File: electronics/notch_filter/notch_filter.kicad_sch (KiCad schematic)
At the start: 39 parts, among them J1 Conn_01x03, J2 Conn_01x03, J3 Output, J4 In, J5 module_2x15_left_input, J6 module_2x15_right_input, U1 opamp_single_8pin

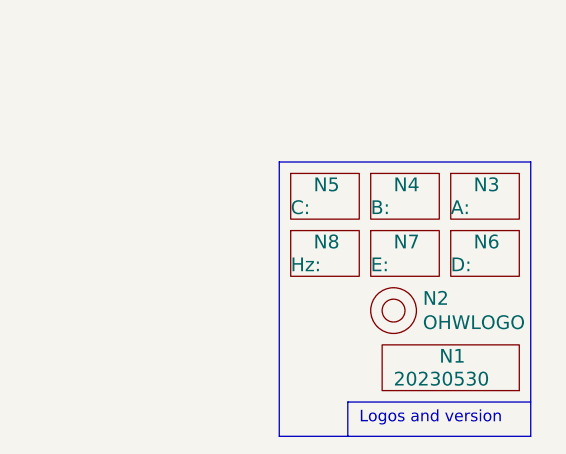
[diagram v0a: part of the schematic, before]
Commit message: removed labels and minor optimisations
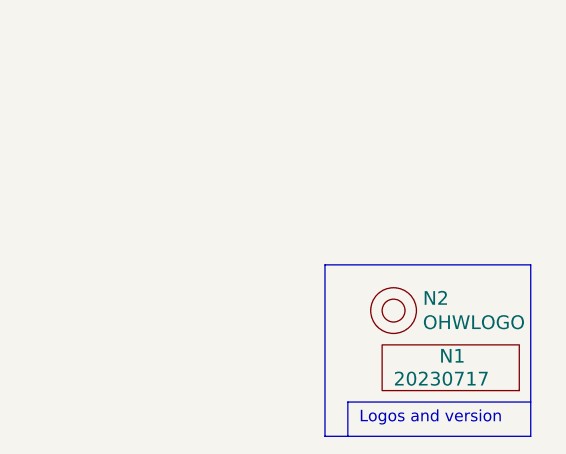
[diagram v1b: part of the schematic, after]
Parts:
- removed N3: A:, SquantorLabels:Label_Note_medium, symbol SquantorLabels:Label
- removed N4: B:, SquantorLabels:Label_Note_medium, symbol SquantorLabels:Label
- removed N5: C:, SquantorLabels:Label_Note_medium, symbol SquantorLabels:Label
- removed N6: D:, SquantorLabels:Label_Note_medium, symbol SquantorLabels:Label
- removed N7: E:, SquantorLabels:Label_Note_medium, symbol SquantorLabels:Label
- removed N8: Hz:, SquantorLabels:Label_Note_medium, symbol SquantorLabels:Label
- N1: value 20230530 -> 20230717
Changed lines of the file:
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@@
     (stroke (width 0) (type default))
   )
-  (polyline (pts (xy 147.32 165.1) (xy 147.32 195.58))
+  (polyline (pts (xy 152.4 176.53) (xy 152.4 195.58))
     (stroke (width 0) (type default))
   )
@@
     (stroke (width 0) (type default))
   )
-  (polyline (pts (xy 175.26 165.1) (xy 147.32 165.1))
+  (polyline (pts (xy 175.26 176.53) (xy 152.4 176.53))
     (stroke (width 0) (type default))
   )
@@
     (stroke (width 0) (type default))
   )
-  (polyline (pts (xy 175.26 195.58) (xy 175.26 165.1))
+  (polyline (pts (xy 175.26 195.58) (xy 175.26 176.53))
     (stroke (width 0) (type default))
   )
@@
     (stroke (width 0) (type default))
   )
-  (polyline (pts (xy 147.32 195.58) (xy 175.26 195.58))
+  (polyline (pts (xy 152.4 195.58) (xy 175.26 195.58))
     (stroke (width 0) (type default))
   )
@@
       (effects (font (size 1.524 1.524)) (justify left))
     )
-    (property "Value" "20230530" (at 160.02 189.23 0)
+    (property "Value" "20230717" (at 160.02 189.23 0)
       (effects (font (size 1.524 1.524)) (justify left))
     )
@@
         (path "/646d9e91-59b4-4865-a2fc-29780ed32563"
           (reference "R2") (unit 1)
-        )
-      )
-    )
-  )
-  (symbol (lib_id "SquantorLabels:Label") (at 152.4 175.26 0) (unit 1)
-    (in_bom yes) (on_board yes) (dnp no)
-    (property "Reference" "N8" (at 151.13 173.99 0)
-      (effects (font (size 1.524 1.524)) (justify left))
-    )
-    (property "Value" "Hz:" (at 148.59 176.53 0)
-      (effects (font (size 1.524 1.524)) (justify left))
-    )
-    (property "Footprint" "SquantorLabels:Label_Note_medium" (at 152.4 175.26 0)
-      (effects (font (size 1.524 1.524)) hide)
-    )
-    (property "Datasheet" "" (at 152.4 175.26 0)
-      (effects (font (size 1.524 1.524)) hide)
-    )
-    (instances
-      (project "notch_filter"
-        (path "/646d9e91-59b4-4865-a2fc-29780ed32563"
-          (reference "N8") (unit 1)
         )
       )
@@
     )
   )
-  (symbol (lib_id "SquantorLabels:Label") (at 152.4 168.91 0) (unit 1)
-    (in_bom yes) (on_board yes) (dnp no)
-    (property "Reference" "N5" (at 151.13 167.64 0)
-      (effects (font (size 1.524 1.524)) (justify left))
-    )
-    (property "Value" "C:" (at 148.59 170.18 0)
-      (effects (font (size 1.524 1.524)) (justify left))
-    )
-    (property "Footprint" "SquantorLabels:Label_Note_medium" (at 152.4 168.91 0)
-      (effects (font (size 1.524 1.524)) hide)
-    )
-    (property "Datasheet" "" (at 152.4 168.91 0)
-      (effects (font (size 1.524 1.524)) hide)
-    )
-    (instances
-      (project "notch_filter"
-        (path "/646d9e91-59b4-4865-a2fc-29780ed32563"
-          (reference "N5") (unit 1)
-        )
-      )
-    )
-  )
   (symbol (lib_id "Device:C") (at 139.7 44.45 90) (unit 1)
     (in_bom yes) (on_board yes) (dnp no)
@@
     )
   )
-  (symbol (lib_id "SquantorLabels:Label") (at 170.18 168.91 0) (unit 1)
-    (in_bom yes) (on_board yes) (dnp no)
-    (property "Reference" "N3" (at 168.91 167.64 0)
-      (effects (font (size 1.524 1.524)) (justify left))
-    )
-    (property "Value" "A:" (at 166.37 170.18 0)
-      (effects (font (size 1.524 1.524)) (justify left))
-    )
-    (property "Footprint" "SquantorLabels:Label_Note_medium" (at 170.18 168.91 0)
-      (effects (font (size 1.524 1.524)) hide)
-    )
-    (property "Datasheet" "" (at 170.18 168.91 0)
-      (effects (font (size 1.524 1.524)) hide)
-    )
-    (instances
-      (project "notch_filter"
-        (path "/646d9e91-59b4-4865-a2fc-29780ed32563"
-          (reference "N3") (unit 1)
-        )
-      )
-    )
-  )
-  (symbol (lib_id "SquantorLabels:Label") (at 170.18 175.26 0) (unit 1)
-    (in_bom yes) (on_board yes) (dnp no)
-    (property "Reference" "N6" (at 168.91 173.99 0)
-      (effects (font (size 1.524 1.524)) (justify left))
-    )
-    (property "Value" "D:" (at 166.37 176.53 0)
-      (effects (font (size 1.524 1.524)) (justify left))
-    )
-    (property "Footprint" "SquantorLabels:Label_Note_medium" (at 170.18 175.26 0)
-      (effects (font (size 1.524 1.524)) hide)
-    )
-    (property "Datasheet" "" (at 170.18 175.26 0)
-      (effects (font (size 1.524 1.524)) hide)
-    )
-    (instances
-      (project "notch_filter"
-        (path "/646d9e91-59b4-4865-a2fc-29780ed32563"
-          (reference "N6") (unit 1)
-        )
-      )
-    )
-  )
-  (symbol (lib_id "SquantorLabels:Label") (at 161.29 175.26 0) (unit 1)
-    (in_bom yes) (on_board yes) (dnp no)
-    (property "Reference" "N7" (at 160.02 173.99 0)
-      (effects (font (size 1.524 1.524)) (justify left))
-    )
-    (property "Value" "E:" (at 157.48 176.53 0)
-      (effects (font (size 1.524 1.524)) (justify left))
-    )
-    (property "Footprint" "SquantorLabels:Label_Note_medium" (at 161.29 175.26 0)
-      (effects (font (size 1.524 1.524)) hide)
-    )
-    (property "Datasheet" "" (at 161.29 175.26 0)
-      (effects (font (size 1.524 1.524)) hide)
-    )
-    (instances
-      (project "notch_filter"
-        (path "/646d9e91-59b4-4865-a2fc-29780ed32563"
-          (reference "N7") (unit 1)
-        )
-      )
-    )
-  )
   (symbol (lib_id "power:GND") (at 73.66 55.88 0) (unit 1)
     (in_bom yes) (on_board yes) (dnp no)
@@
         )
       )
-    )
-  )
-  (symbol (lib_id "SquantorLabels:Label") (at 161.29 168.91 0) (unit 1)
-    (in_bom yes) (on_board yes) (dnp no)
-    (property "Reference" "N4" (at 160.02 167.64 0)
-      (effects (font (size 1.524 1.524)) (justify left))
-    )
-    (property "Value" "B:" (at 157.48 170.18 0)
-      (effects (font (size 1.524 1.524)) (justify left))
-    )
-    (property "Footprint" "SquantorLabels:Label_Note_medium" (at 161.29 168.91 0)
-      (effects (font (size 1.524 1.524)) hide)
-    )
-    (property "Datasheet" "" (at 161.29 168.91 0)
-      (effects (font (size 1.524 1.524)) hide)
-    )
-    (instances
-      (project "notch_filter"
-        (path "/646d9e91-59b4-4865-a2fc-29780ed32563"
-          (reference "N4") (unit 1)
-        )
-      )
